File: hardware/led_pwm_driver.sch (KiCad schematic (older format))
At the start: 1 part, among them U1 74AHCT1G125

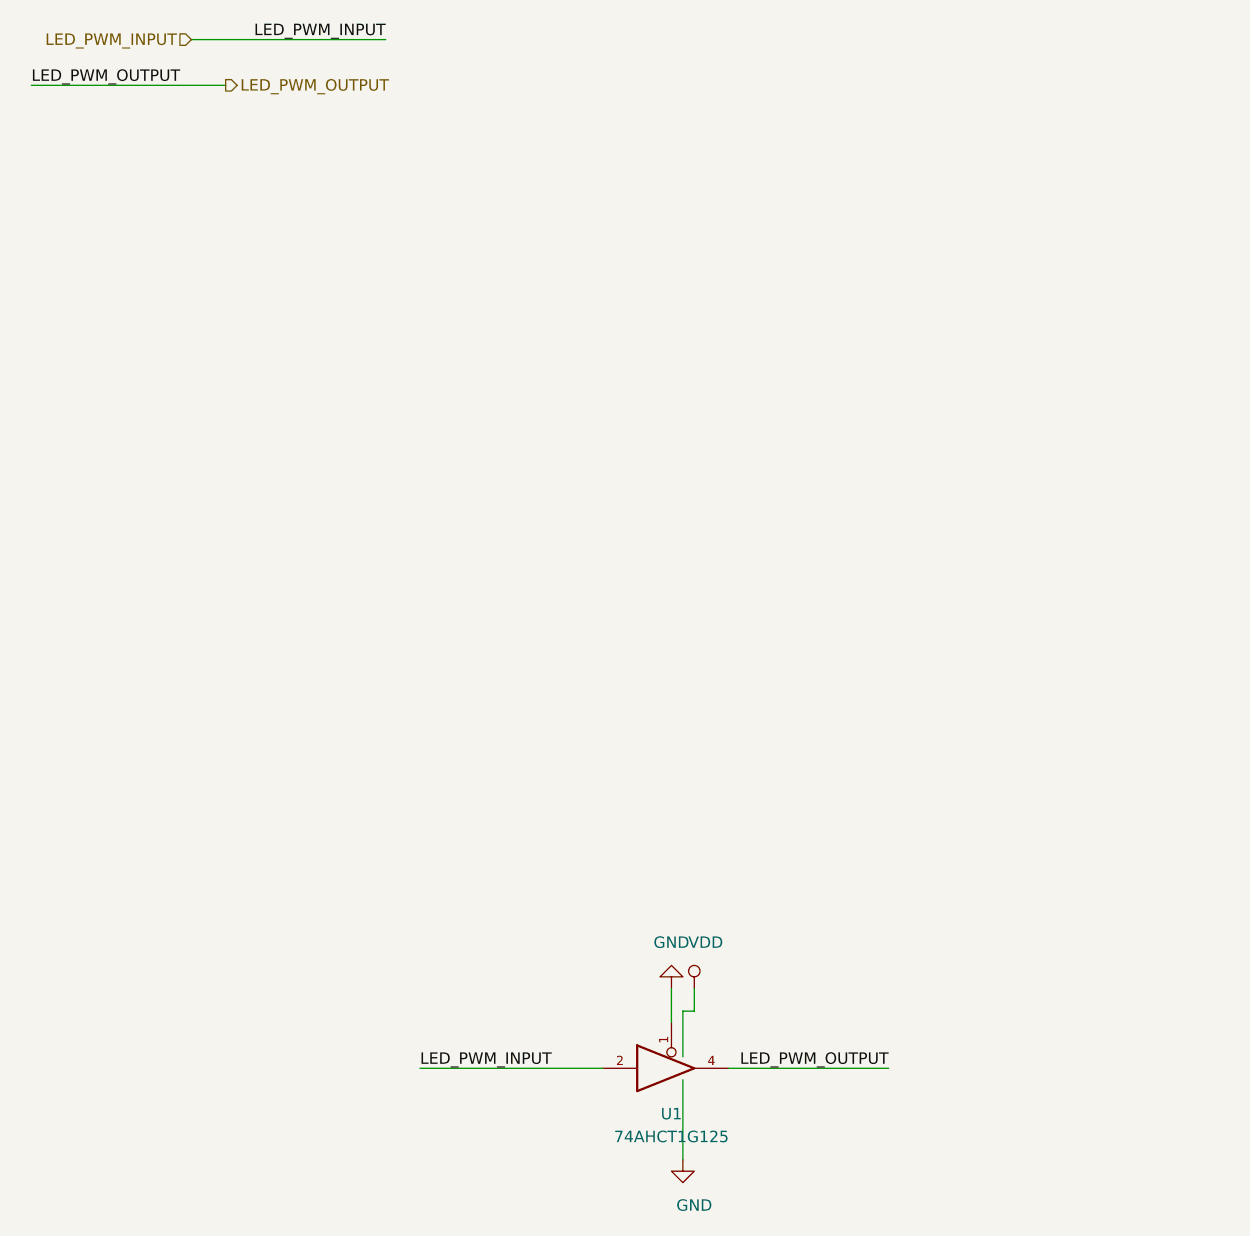
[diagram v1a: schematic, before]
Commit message: update WS2812\,
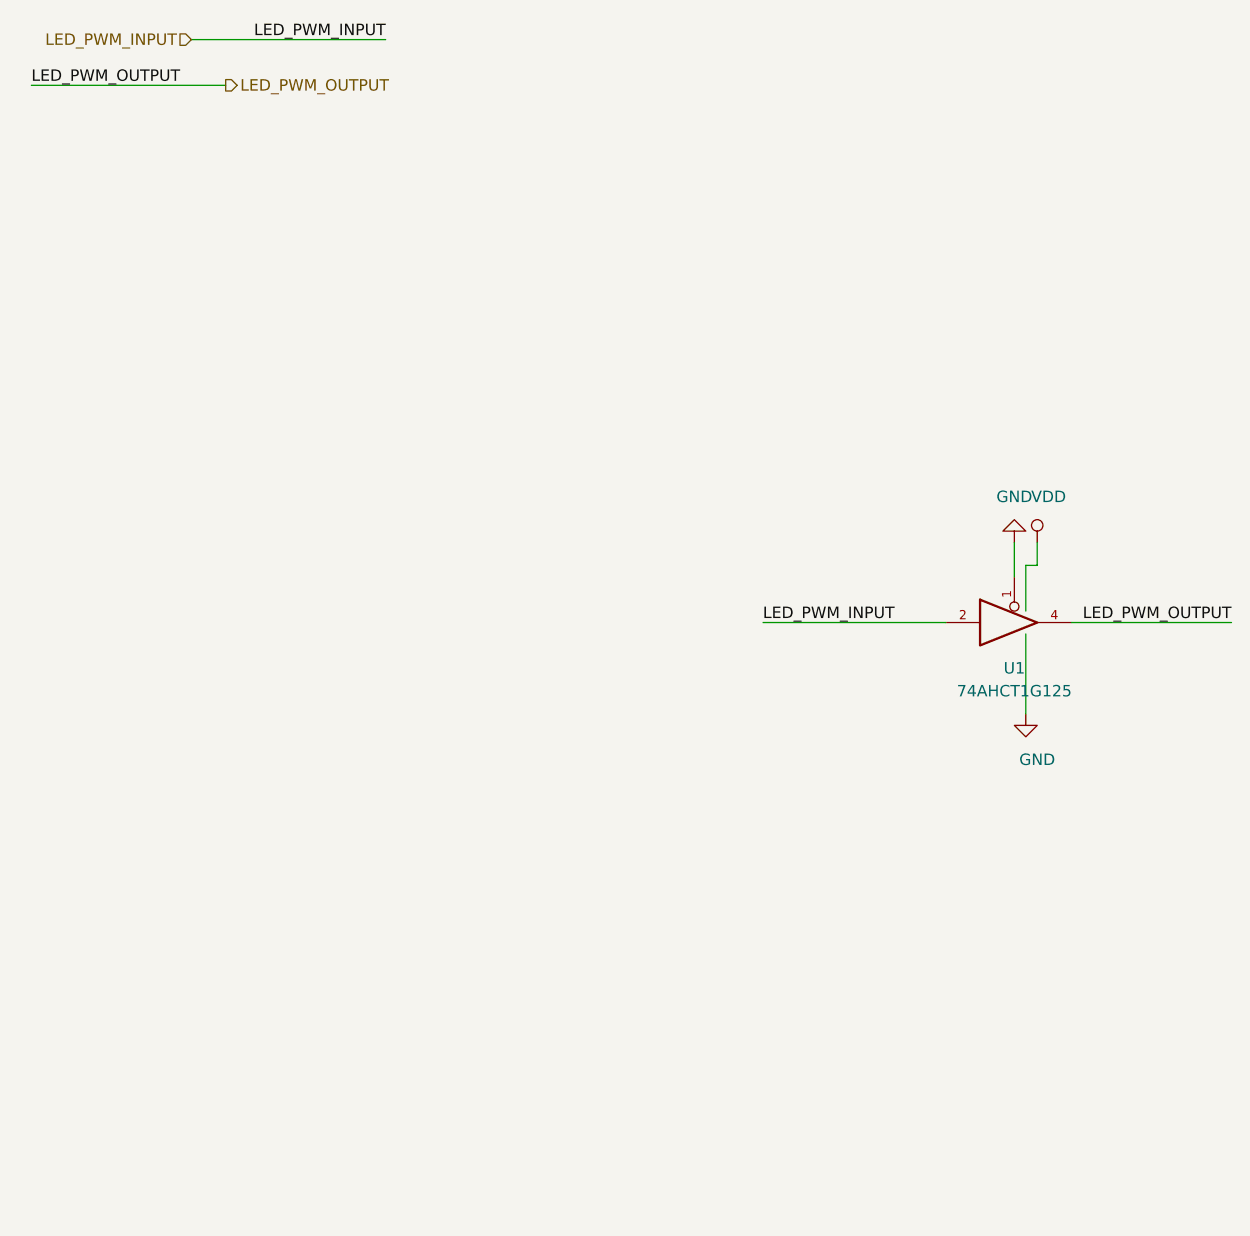
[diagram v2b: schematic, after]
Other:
- moved on the sheet: U1
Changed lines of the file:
@@
 $Descr A4 11693 8268
 encoding utf-8
-Sheet 8 12
+Sheet 11 11
 Title ""
 Date ""
@@
 L taobao-components:74AHCT1G125 U?
 U 1 1 5CD3E9C8
-P 4250 5500
+P 5750 3550
 AR Path="/5CD03534/5CD3E9C8" Ref="U?"  Part="1"
 AR Path="/5CD44B8D/5CD3E9C8" Ref="U1"  Part="1"
-F 0 "U1" H 4250 5300 50  0000 C CNN
-F 1 "74AHCT1G125" H 4250 5200 50  0000 C CNN
-F 2 "Package_TO_SOT_SMD:SOT-23-5_HandSoldering" H 4250 5500 50  0001 C CNN
-F 3 "" H 4250 5500 50  0001 C CNN
-	1    4250 5500
+F 0 "U1" H 5750 3350 50  0000 C CNN
+F 1 "74AHCT1G125" H 5750 3250 50  0000 C CNN
+F 2 "Package_TO_SOT_SMD:SOT-23-5_HandSoldering" H 5750 3550 50  0001 C CNN
+F 3 "" H 5750 3550 50  0001 C CNN
+	1    5750 3550
 	1    0    0    -1
 $EndComp
-Text Label 3150 5500 0    50   ~ 0
+Text Label 4650 3550 0    50   ~ 0
 LED_PWM_INPUT
-Text Label 5200 5500 2    50   ~ 0
+Text Label 6700 3550 2    50   ~ 0
 LED_PWM_OUTPUT
 $Comp
 L power:VDD #PWR?
 U 1 1 5CD3EB2F
-P 4350 5150
+P 5850 3200
 AR Path="/5CD03534/5CD3EB2F" Ref="#PWR?"  Part="1"
 AR Path="/5CD44B8D/5CD3EB2F" Ref="#PWR0519"  Part="1"
-F 0 "#PWR0519" H 4350 5000 50  0001 C CNN
-F 1 "VDD" H 4400 5350 50  0000 C CNN
-F 2 "" H 4350 5150 50  0001 C CNN
-F 3 "" H 4350 5150 50  0001 C CNN
-	1    4350 5150
+F 0 "#PWR0519" H 5850 3050 50  0001 C CNN
+F 1 "VDD" H 5900 3400 50  0000 C CNN
+F 2 "" H 5850 3200 50  0001 C CNN
+F 3 "" H 5850 3200 50  0001 C CNN
+	1    5850 3200
 	1    0    0    -1
 $EndComp
@@
 L power:GND #PWR?
 U 1 1 5CD3ED3F
-P 4250 5150
+P 5750 3200
 AR Path="/5CD03534/5CD3ED3F" Ref="#PWR?"  Part="1"
 AR Path="/5CD44B8D/5CD3ED3F" Ref="#PWR0518"  Part="1"
-F 0 "#PWR0518" H 4250 4900 50  0001 C CNN
-F 1 "GND" H 4250 4950 50  0000 C CNN
-F 2 "" H 4250 5150 50  0001 C CNN
-F 3 "" H 4250 5150 50  0001 C CNN
-	1    4250 5150
+F 0 "#PWR0518" H 5750 2950 50  0001 C CNN
+F 1 "GND" H 5750 3000 50  0000 C CNN
+F 2 "" H 5750 3200 50  0001 C CNN
+F 3 "" H 5750 3200 50  0001 C CNN
+	1    5750 3200
 	-1   0    0    1
 $EndComp
@@
 L power:GND #PWR?
 U 1 1 5CD3F2FC
-P 4300 5900
+P 5800 3950
 AR Path="/5CD03534/5CD3F2FC" Ref="#PWR?"  Part="1"
 AR Path="/5CD44B8D/5CD3F2FC" Ref="#PWR0520"  Part="1"
-F 0 "#PWR0520" H 4300 5650 50  0001 C CNN
-F 1 "GND" H 4350 5700 50  0000 C CNN
-F 2 "" H 4300 5900 50  0001 C CNN
-F 3 "" H 4300 5900 50  0001 C CNN
-	1    4300 5900
+F 0 "#PWR0520" H 5800 3700 50  0001 C CNN
+F 1 "GND" H 5850 3750 50  0000 C CNN
+F 2 "" H 5800 3950 50  0001 C CNN
+F 3 "" H 5800 3950 50  0001 C CNN
+	1    5800 3950
 	1    0    0    -1
 $EndComp
 Wire Wire Line
-	4300 5550 4300 5900
+	5800 3600 5800 3950
 Wire Wire Line
-	4250 5150 4250 5300
+	5750 3200 5750 3350
 Wire Wire Line
-	4350 5150 4350 5250
+	5850 3200 5850 3300
 Wire Wire Line
-	4350 5250 4300 5250
+	5850 3300 5800 3300
 Wire Wire Line
-	4300 5250 4300 5450
+	5800 3300 5800 3500
 Wire Wire Line
-	4500 5500 5200 5500
+	6000 3550 6700 3550
 Wire Wire Line
-	3150 5500 3950 5500
+	4650 3550 5450 3550
 Text HLabel 2300 1200 2    50   Output ~ 0
 LED_PWM_OUTPUT

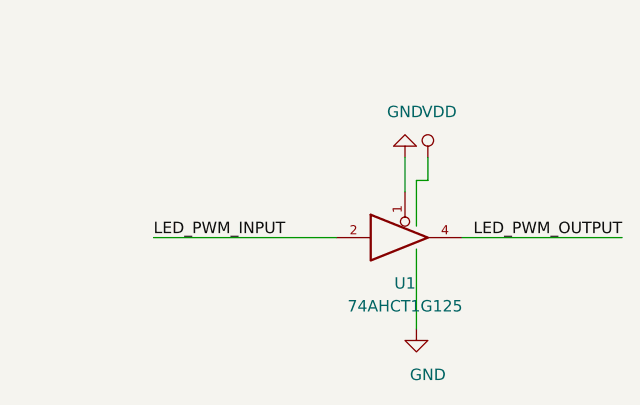
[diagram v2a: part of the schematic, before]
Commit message: update WS2812\,
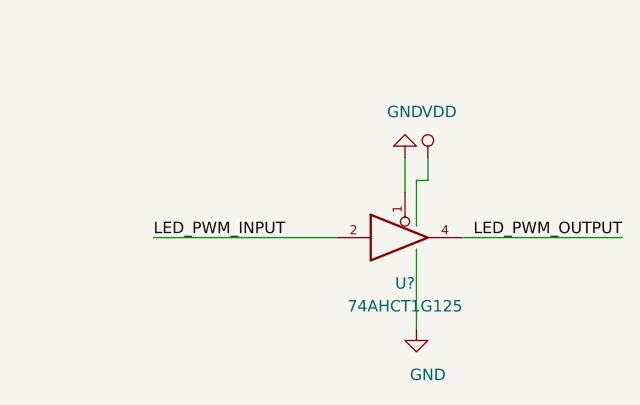
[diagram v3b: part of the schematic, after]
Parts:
- renumbered U1 to U?
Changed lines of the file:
@@
 P 5750 3550
 AR Path="/5CD03534/5CD3E9C8" Ref="U?"  Part="1"
-AR Path="/5CD44B8D/5CD3E9C8" Ref="U1"  Part="1"
-F 0 "U1" H 5750 3350 50  0000 C CNN
+AR Path="/5CD44B8D/5CD3E9C8" Ref="U?"  Part="1"
+F 0 "U?" H 5750 3350 50  0000 C CNN
 F 1 "74AHCT1G125" H 5750 3250 50  0000 C CNN
 F 2 "Package_TO_SOT_SMD:SOT-23-5_HandSoldering" H 5750 3550 50  0001 C CNN
@@
 P 5850 3200
 AR Path="/5CD03534/5CD3EB2F" Ref="#PWR?"  Part="1"
-AR Path="/5CD44B8D/5CD3EB2F" Ref="#PWR0519"  Part="1"
-F 0 "#PWR0519" H 5850 3050 50  0001 C CNN
+AR Path="/5CD44B8D/5CD3EB2F" Ref="#PWR?"  Part="1"
+F 0 "#PWR?" H 5850 3050 50  0001 C CNN
 F 1 "VDD" H 5900 3400 50  0000 C CNN
 F 2 "" H 5850 3200 50  0001 C CNN
@@
 P 5750 3200
 AR Path="/5CD03534/5CD3ED3F" Ref="#PWR?"  Part="1"
-AR Path="/5CD44B8D/5CD3ED3F" Ref="#PWR0518"  Part="1"
-F 0 "#PWR0518" H 5750 2950 50  0001 C CNN
+AR Path="/5CD44B8D/5CD3ED3F" Ref="#PWR?"  Part="1"
+F 0 "#PWR?" H 5750 2950 50  0001 C CNN
 F 1 "GND" H 5750 3000 50  0000 C CNN
 F 2 "" H 5750 3200 50  0001 C CNN
@@
 P 5800 3950
 AR Path="/5CD03534/5CD3F2FC" Ref="#PWR?"  Part="1"
-AR Path="/5CD44B8D/5CD3F2FC" Ref="#PWR0520"  Part="1"
-F 0 "#PWR0520" H 5800 3700 50  0001 C CNN
+AR Path="/5CD44B8D/5CD3F2FC" Ref="#PWR?"  Part="1"
+F 0 "#PWR?" H 5800 3700 50  0001 C CNN
 F 1 "GND" H 5850 3750 50  0000 C CNN
 F 2 "" H 5800 3950 50  0001 C CNN
